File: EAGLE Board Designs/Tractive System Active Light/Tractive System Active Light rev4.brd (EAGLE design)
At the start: 67.5 x 26.9 mm, 10 parts, among them J1 CONNECTOR-4_μF_S_RA_

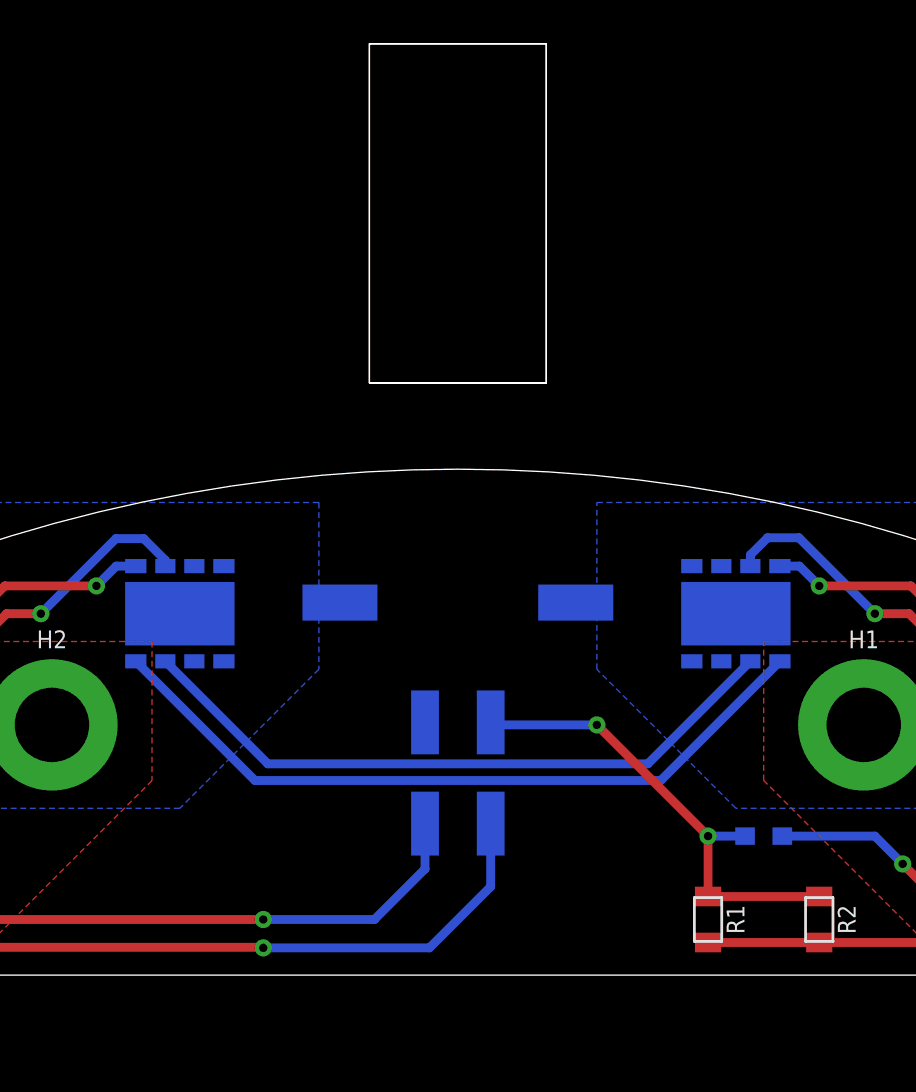
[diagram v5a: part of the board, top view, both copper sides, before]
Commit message: Looks good fixing silkscreen
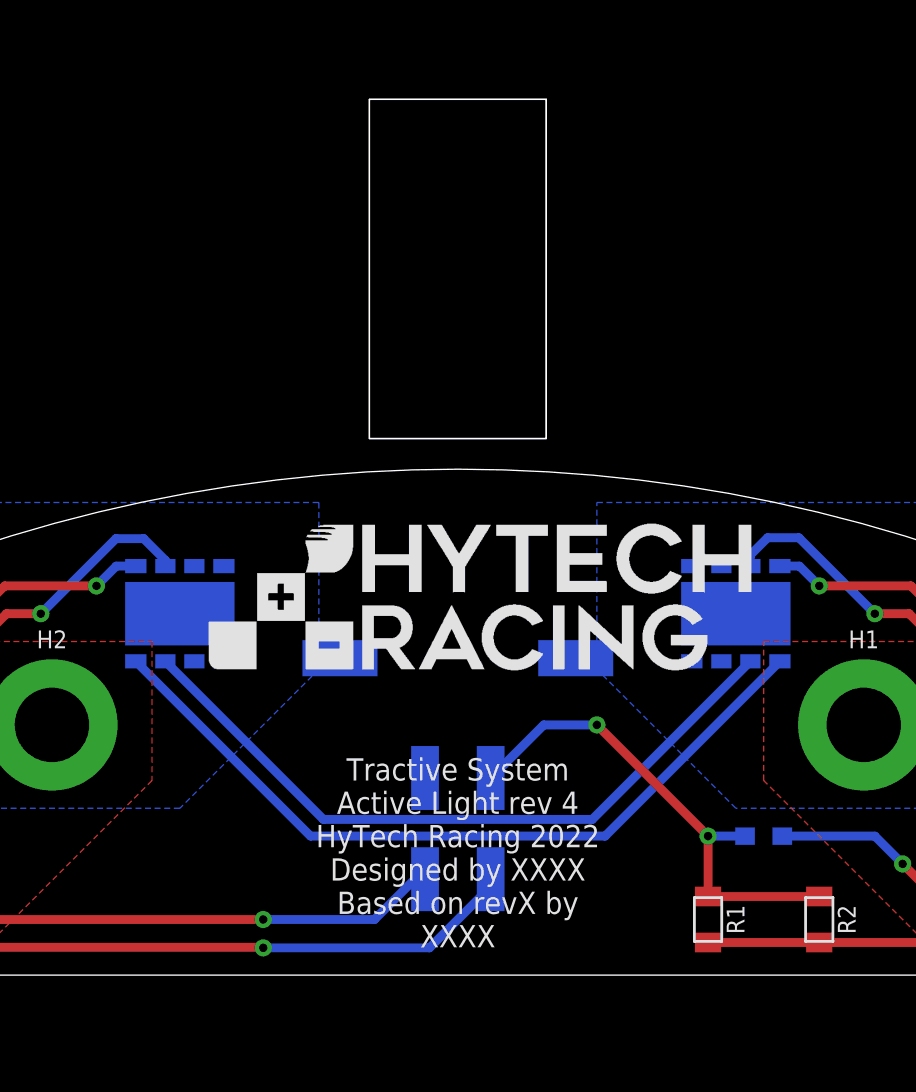
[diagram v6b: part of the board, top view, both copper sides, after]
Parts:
- added U$1: (no value), HyTechManufacturing:LOGO_HYTECH_SQUARE_EXTRA_LARGE
- added U$2: (no value), HyTechManufacturing:LOGO_HYTECH_MEDIUM
- added U$3: (no value), HyTechManufacturing:LOGO_GT_MEDIUM
- moved J1 2.54 mm to (0.00, 14.5)
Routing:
- net GND_RED: track 37.2 -> 34.7 mm
- net GND_GREEN: track 31.4 -> 29.1 mm
- net N$3: track 33.9 -> 36.0 mm
- net N$4: track 30.6 -> 32.7 mm
- net +12V: track 21.6 -> 22.6 mm
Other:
- board text added: "Tractive System Active Light rev 4 HyTech Racing 2022 Designed by XXXX Based on revX by XXXX"

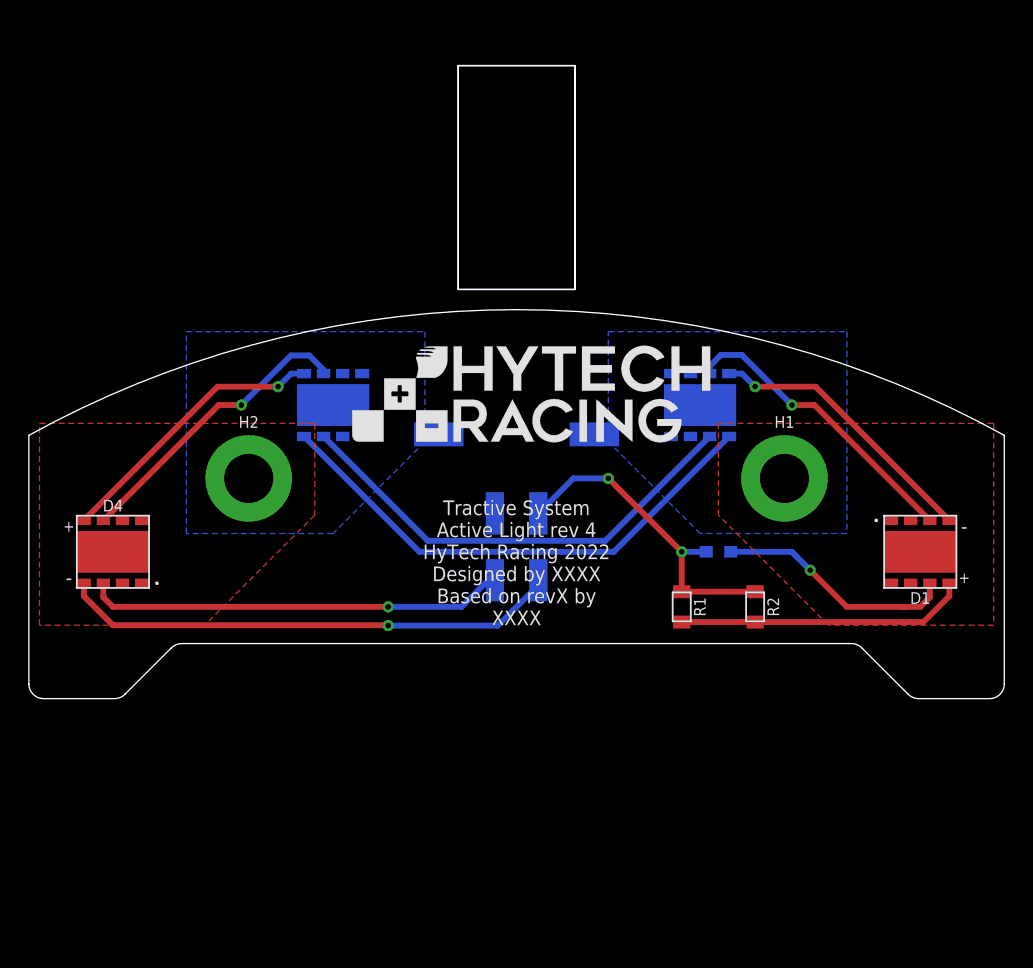
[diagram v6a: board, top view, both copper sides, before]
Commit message: moved mounting hole to not block led
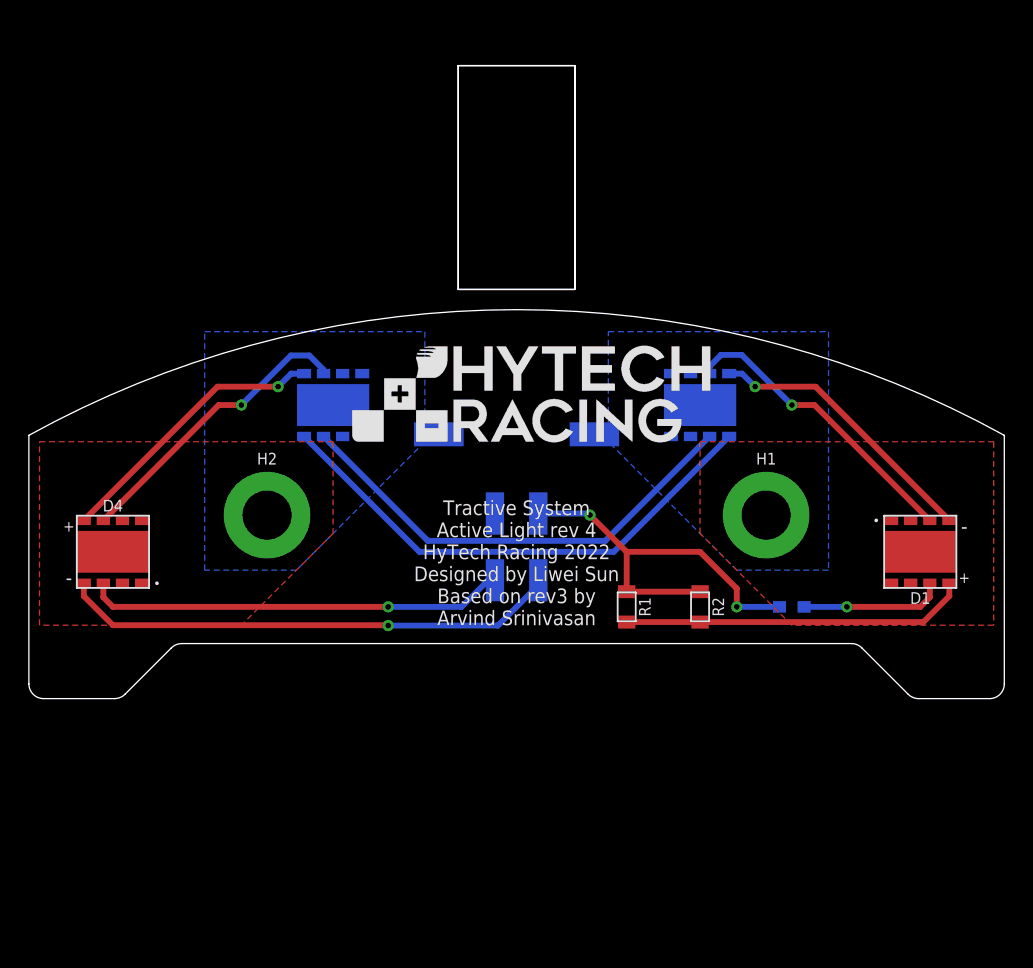
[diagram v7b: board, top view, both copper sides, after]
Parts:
- moved R3 6.35 mm to (19.1, 2.54)
- moved R2 3.81 mm to (12.7, 2.54)
- moved R1 3.81 mm to (7.62, 2.54)
- moved H1 2.84 mm to (17.3, 8.89)
- moved H2 2.84 mm to (-17.3, 8.89)
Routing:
- net N$9: track 16.6 -> 9.95 mm
- net +12V: track 22.6 -> 28.0 mm
- net N$7: track 20.2 -> 24.0 mm
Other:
- board text added: "Tractive System Active Light rev 4 HyTech Racing 2022 Designed by Liwei Sun Based on rev3 by Arvind Srinivasan"
- board text removed: "Tractive System Active Light rev 4 HyTech Racing 2022 Designed by XXXX Based on revX by XXXX"

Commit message: Tsal mech electrical reconciliation (#31)
* edited LED and mounting hole positions, added DXF

* order files
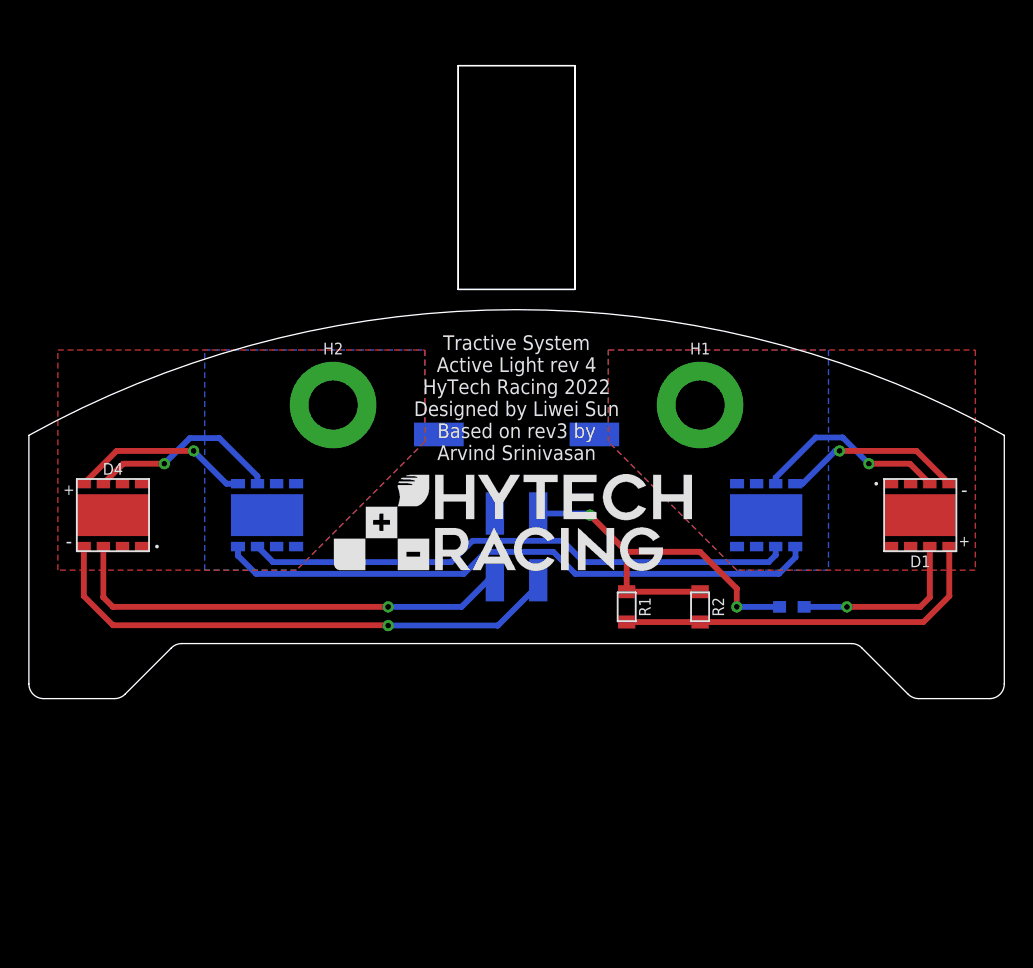
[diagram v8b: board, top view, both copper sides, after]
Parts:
- moved U$2 8.98 mm to (-12.7, 5.08)
- moved D2 8.89 mm to (17.3, 8.89)
- moved D3 8.89 mm to (-17.3, 8.89)
- moved H1 8.89 mm to (12.7, 16.5)
- moved H2 8.89 mm to (-12.7, 16.5)
- moved D1 2.54 mm to (27.9, 8.89)
- moved D4 2.54 mm to (-27.9, 8.89)
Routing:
- net N$6: track 20.8 -> 13.6 mm
- net N$2: track 20.6 -> 13.6 mm
- net N$5: track 19.4 -> 12.5 mm
- net N$1: track 19.4 -> 12.5 mm
- net N$3: track 36.0 -> 42.2 mm
- net N$4: track 32.7 -> 38.3 mm
- net GND_RED: track 34.7 -> 37.2 mm
- net N$7: track 24.0 -> 26.5 mm
- net N$9: track 9.95 -> 12.5 mm
- net GND_GREEN: track 29.1 -> 31.7 mm
